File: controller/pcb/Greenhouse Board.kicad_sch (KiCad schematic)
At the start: 9 parts, among them J1 window_control, J2 fan_control, J3 temp_humidity_sensor, J4 misc_sensor_1, J5 misc_sensor_2, Q1 Q_NMOS_GDS, Q2 Q_NMOS_GDS, U1 ESP32-DEVKITC-32D

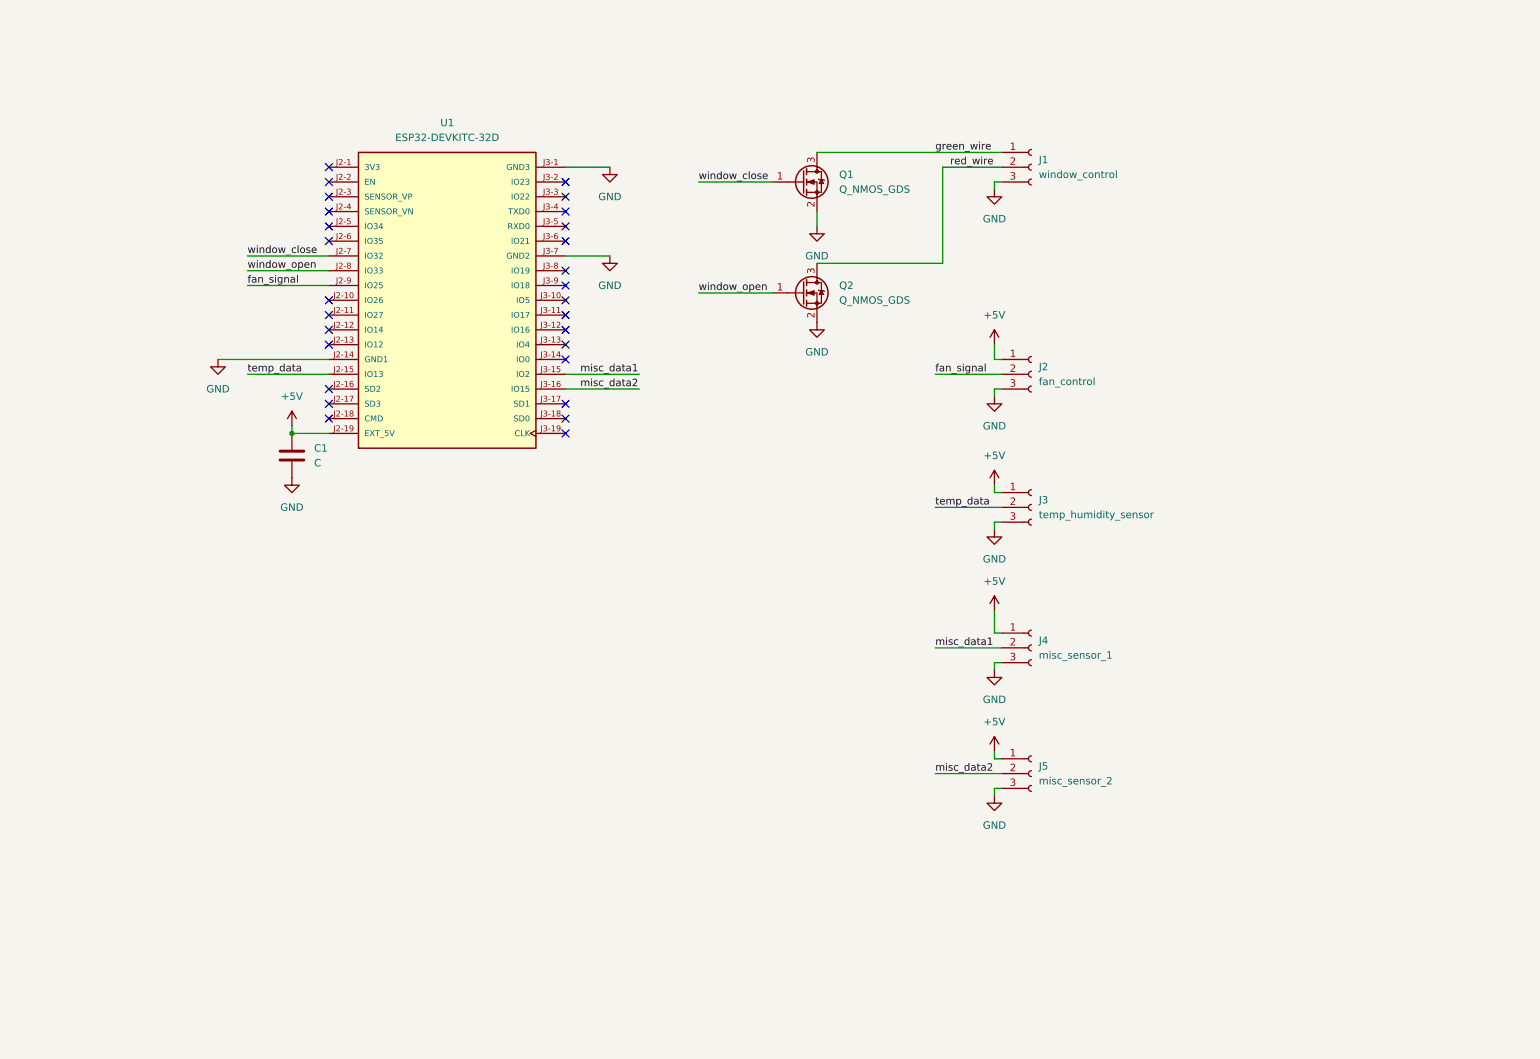
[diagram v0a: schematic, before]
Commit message: Introduce 1/8" jack components and add additional inputs and outputs
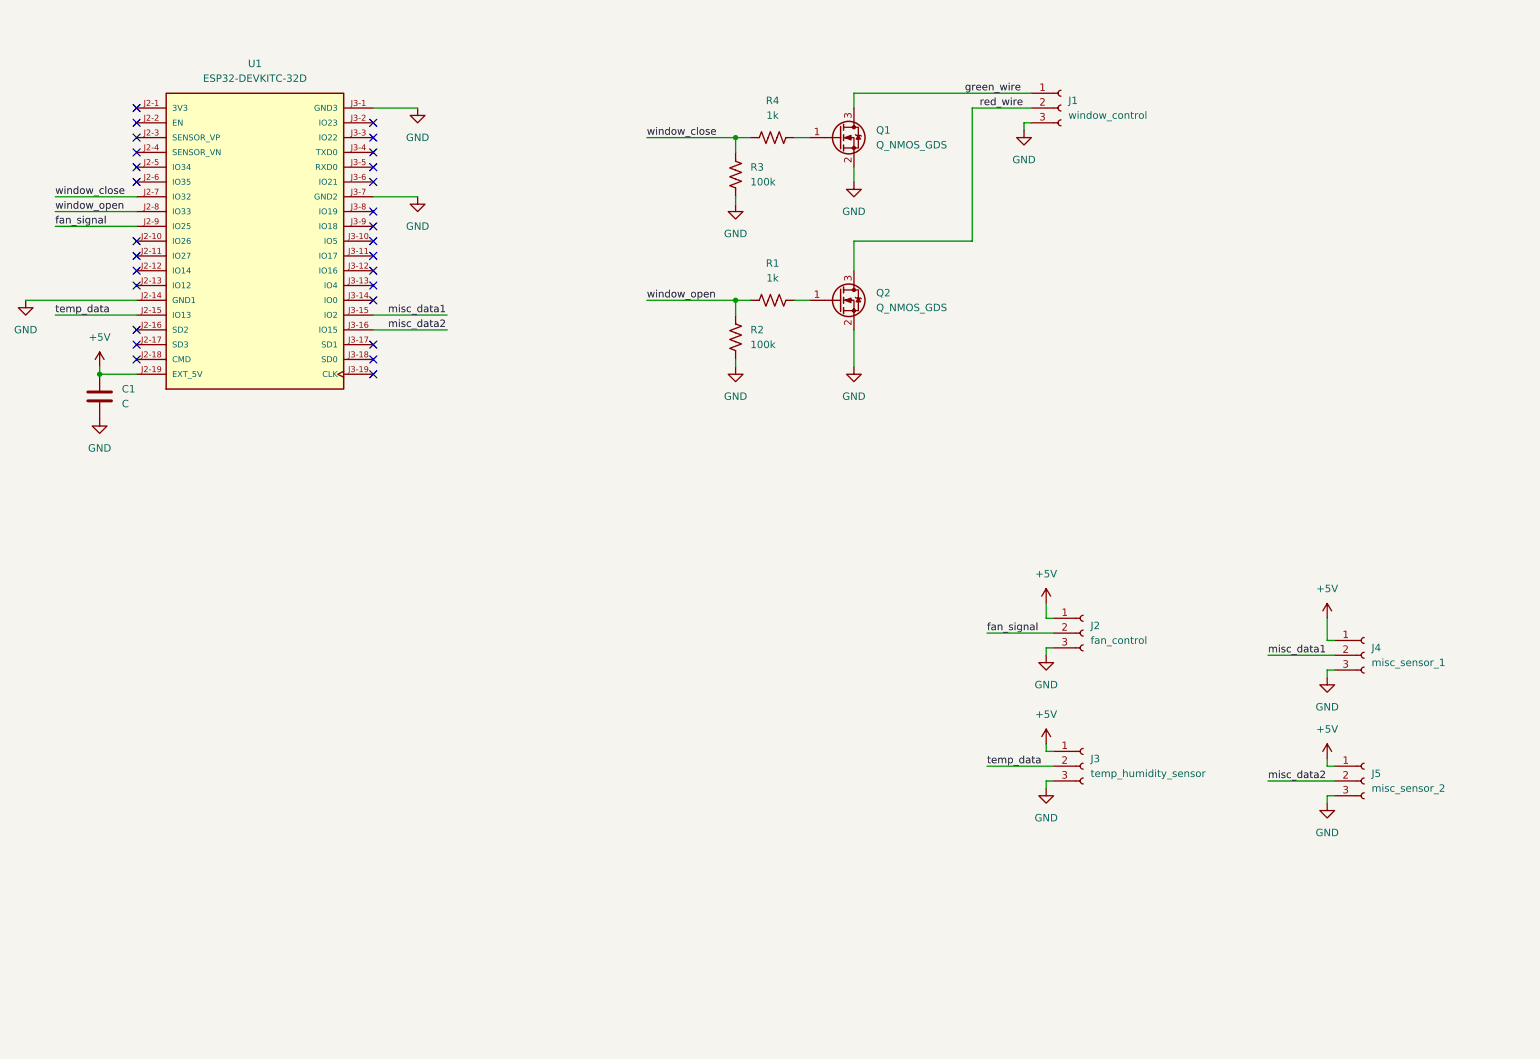
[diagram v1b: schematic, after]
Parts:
- added R1, R4: 1k, symbol Device:R_US
- added R2, R3: 100k, symbol Device:R_US
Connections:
- net GND: now also R2.2, R3.2
- net window_close: now also R3.1, R4.1; no longer Q1.1 (G)
- net window_open: now also R1.1, R2.1; no longer Q2.1 (G)
- new net: Q1.1 (G), R4.2
- new net: Q2.1 (G), R1.2
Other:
- moved on the sheet: C1, J1, J2, J3, J4, J5, Q1, Q2, U1

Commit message: Updates to the PCB to expand its inputs/outputs
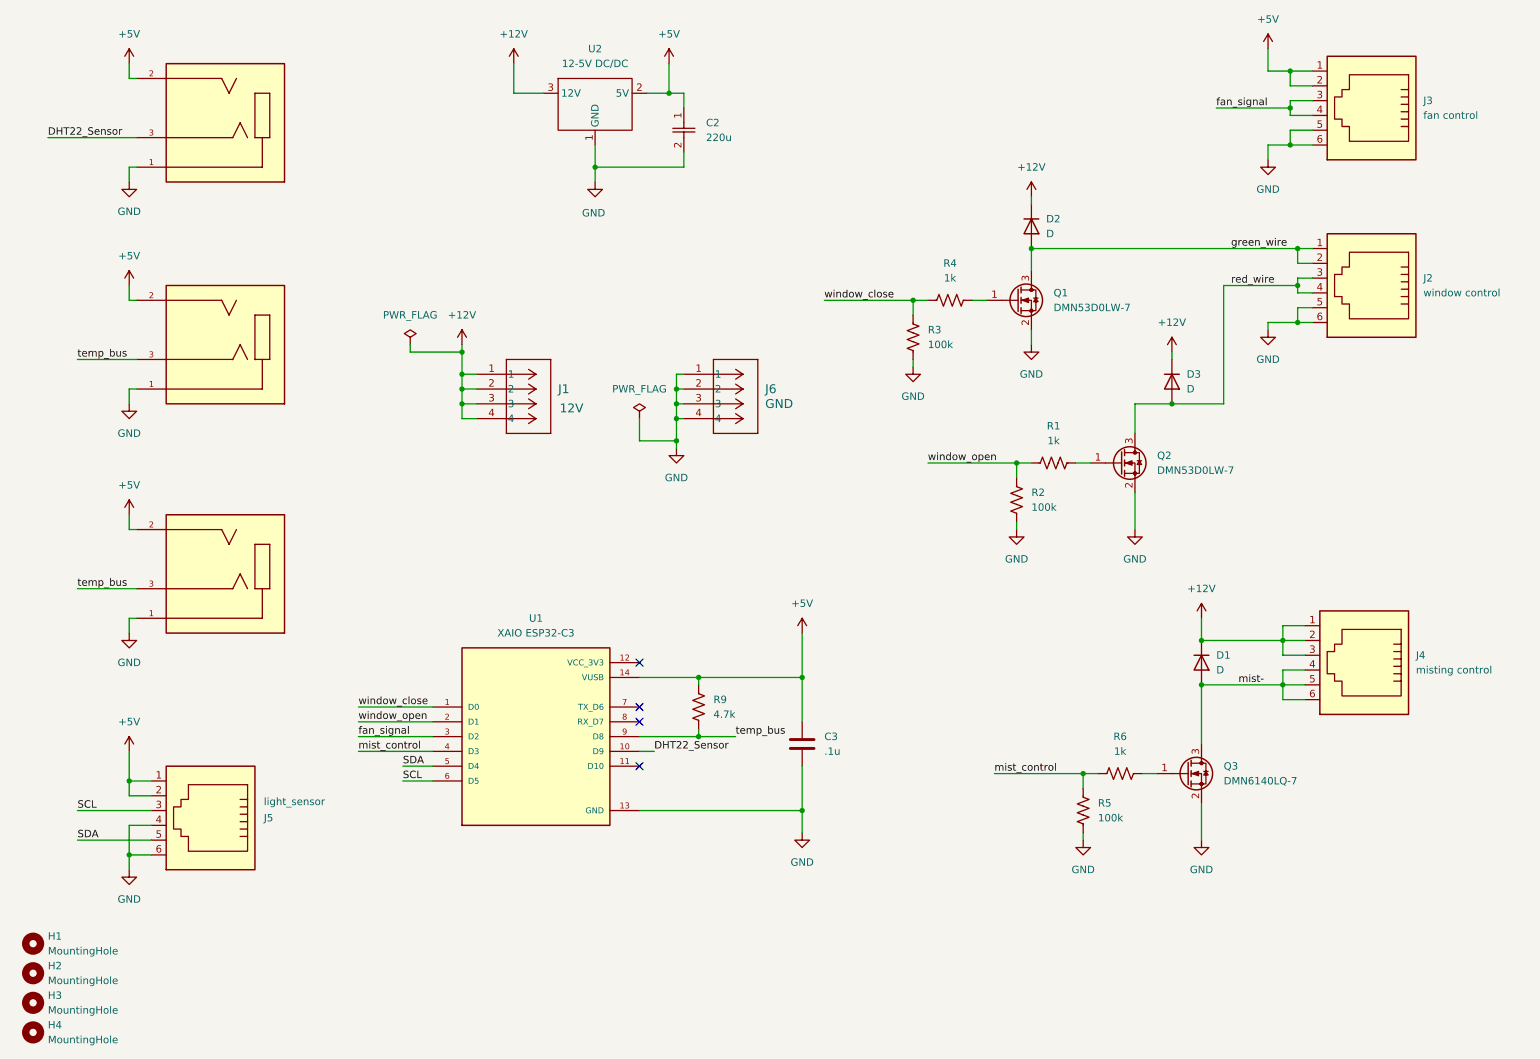
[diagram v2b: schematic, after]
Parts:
- removed C1: C, Capacitor_SMD:C_0805_2012Metric, symbol Device:C
- removed J1: window_control, Connector_PinSocket_2.54mm:PinSocket_1x03_P2.54mm_Vertical, symbol Connector:Conn_01x03_Socket
- removed J2: fan_control, Connector_PinSocket_2.54mm:PinSocket_1x03_P2.54mm_Vertical, symbol Connector:Conn_01x03_Socket
- removed J3: temp_humidity_sensor, Connector_PinSocket_2.54mm:PinSocket_1x03_P2.54mm_Vertical, symbol Connector:Conn_01x03_Socket
- removed J4: misc_sensor_1, Connector_PinSocket_2.54mm:PinSocket_1x03_P2.54mm_Vertical, symbol Connector:Conn_01x03_Socket
- removed J5: misc_sensor_2, Connector_PinSocket_2.54mm:PinSocket_1x03_P2.54mm_Vertical, symbol Connector:Conn_01x03_Socket
- removed U1: ESP32-DEVKITC-32D, ESP32-DEVKITC-32D:MODULE_ESP32-DEVKITC-32D, symbol ESP32-DEVKITC-32D:ESP32-DEVKITC-32D
- added C2: 220u, Garth:CAP_SP-CAP_SR_PAN, symbol Garth Libraries:EEF-SR0D221R4
- added C3: .1u, Capacitor_SMD:C_0805_2012Metric, symbol Device:C
- added D1, D2, D3: D, Garth:SOD323_DIO, symbol Device:D
- added H1, H2, H3, H4: MountingHole, MountingHole:MountingHole_3.2mm_M3, symbol Mechanical:MountingHole
- added J1: 12V, Garth:screw-terminal-CONN4_TB002-500_787x299_CUD, symbol Garth Libraries:screw-terminal-TB002-500-04BE
- added J2: window control, Garth:RJ11-RA, symbol Connector:RJ12
- added J3: fan control, Garth:RJ11-RA, symbol Connector:RJ12
- added J4: misting control, Garth:RJ11-RA, symbol Connector:RJ12
- added J5: light_sensor, Garth:RJ11-RA, symbol Connector:RJ12
- added J6: GND, Garth:screw-terminal-CONN4_TB002-500_787x299_CUD, symbol Garth Libraries:screw-terminal-TB002-500-04BE
- added J7: T+H sensor, Garth:1_8jack-CUI_SJ2-35853A-SMT-TR, symbol Garth Libraries:1_8jack-SJ2-35853A-SMT-TR
- added J8: temp sensor 1, Garth:1_8jack-CUI_SJ2-35853A-SMT-TR, symbol Garth Libraries:1_8jack-SJ2-35853A-SMT-TR
- added J9: temp sensor 2, Garth:1_8jack-CUI_SJ2-35853A-SMT-TR, symbol Garth Libraries:1_8jack-SJ2-35853A-SMT-TR
- added Q3: DMN6140LQ-7, Package_TO_SOT_SMD:SOT-323_SC-70_Handsoldering, symbol Transistor_FET:Q_NMOS_GSD
- added R5: 100k, Resistor_SMD:R_0805_2012Metric_Pad1.20x1.40mm_HandSolder, symbol Device:R_US
- added R6: 1k, Resistor_SMD:R_0805_2012Metric_Pad1.20x1.40mm_HandSolder, symbol Device:R_US
- added R9: 4.7k, Resistor_SMD:R_0805_2012Metric_Pad1.20x1.40mm_HandSolder, symbol Device:R_US
- added U1: XAIO ESP32-C3, Garth:MODULE_113991054, symbol Garth Libraries:ESP32-C3
- added U2: 12-5V DC/DC, Garth:Power Module 6-pin, symbol Garth Libraries:12-5-DC/DC
- Q1, Q2: value Q_NMOS_GDS -> DMN53D0LW-7; symbol Device:Q_NMOS_GSD -> Transistor_FET:Q_NMOS_GSD
- R1, R2, R3, R4: footprint (none) -> Resistor_SMD:R_0805_2012Metric_Pad1.20x1.40mm_HandSolder
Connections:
- net +5V: now also C2.1, C3.1, J3.1, J3.2, J5.1, J5.2, J7.2, J8.2, J9.2, R9.1, U1.14 (VUSB), U2.2 (5V)
- net GND: now also C2.2, C3.2, J2.5, J2.6, J3.5, J3.6, J5.4, J5.6, J6.1, J6.2, J6.3, J6.4, J7.1, J8.1, J9.1, Q3.2 (S), R5.2, U1.13 (GND), U2.1 (GND)
- net fan_signal: now also J3.3, J3.4, U1.3 (D2)
- net green_wire: now also D2.2 (A), J2.1, J2.2
- net red_wire: now also D3.2 (A), J2.3, J2.4
- net window_close: now also U1.1 (D0)
- net window_open: now also U1.2 (D1)
- new net: Q3.1 (G), R6.2
- new net +12V: D1.1 (K), D2.1 (K), D3.1 (K), J1.1, J1.2, J1.3, J1.4, J4.1, J4.2, J4.3, U2.3 (12V)
- new net DHT22_Sensor: J7.3, U1.10 (D9)
- new net SCL: J5.3, U1.6 (D5)
- new net SDA: J5.5, U1.5 (D4)
- new net mist-: D1.2 (A), J4.4, J4.5, J4.6, Q3.3 (D)
- new net mist_control: R5.1, R6.1, U1.4 (D3)
- new net temp_bus: J8.3, J9.3, R9.2, U1.9 (D8)
- no-connect marks 28 -> 4
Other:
- moved on the sheet: Q1, Q2, R1, R2, R3, R4
